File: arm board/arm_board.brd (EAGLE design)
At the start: 76.2 x 159.1 mm, 119 parts, among them J1 APPPP45_PCB_HORIZ_RIGHT, J10 SL02, J11 SL02, J12 SL02, J17 APPPP45_PCB_HORIZ_RIGHT, J18 APPPP45_PCB_HORIZ_RIGHT, J19 ENCODER, J2 APPPP45_PCB_HORIZ_RIGHT, J20 ENCODER, J21 ENCODER, J22 ENCODER, J24 ENCODER, J3 APPPP45_PCB_HORIZ_RIGHT, J5 SERVOMOLEX_SL_VERT_TH, J6 SL02, J7 SL02, J8 SL02, J9 SL02, Q1 Q_IRF7437SMD, U1 TIVA-1294

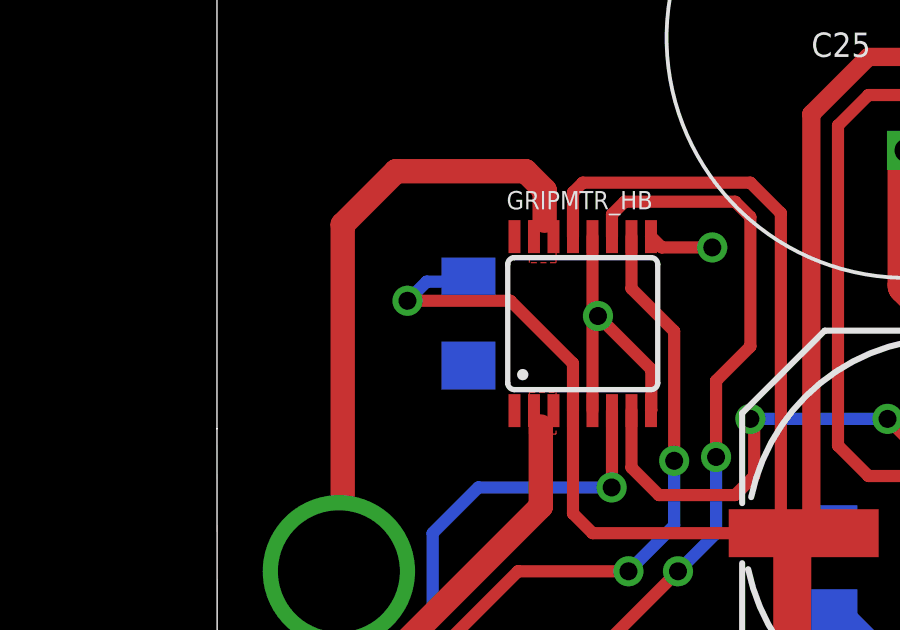
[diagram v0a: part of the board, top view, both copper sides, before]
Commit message: Routed GripHBridge COM pins to ground
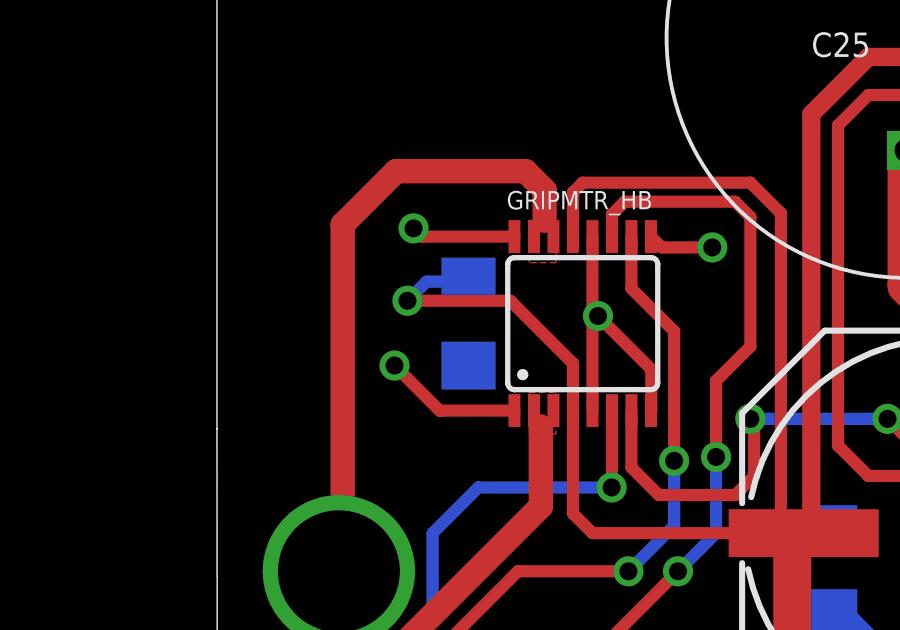
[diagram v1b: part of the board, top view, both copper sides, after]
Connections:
- net GND: now also GRIPMTR_HB.1, GRIPMTR_HB.16
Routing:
- net GND: track 169.0 -> 177.1 mm, vias 82 -> 84
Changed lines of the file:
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@@
 <wire x1="38.0748" y1="86.36" x2="37.4398" y2="86.995" width="0.8128" layer="1"/>
 <wire x1="37.4398" y1="86.995" x2="36.2458" y2="86.995" width="0.8128" layer="1"/>
+<contactref element="GRIPMTR_HB" pad="1"/>
+<contactref element="GRIPMTR_HB" pad="16"/>
+<wire x1="9.7138" y1="136.165" x2="7.218" y2="136.165" width="0.4064" layer="1"/>
+<wire x1="7.218" y1="136.165" x2="5.715" y2="137.668" width="0.4064" layer="1"/>
+<via x="5.715" y="137.668" extent="1-16" drill="0.6" shape="square"/>
+<wire x1="9.7138" y1="141.965" x2="6.625" y2="141.965" width="0.4064" layer="1"/>
+<wire x1="6.625" y1="141.965" x2="6.35" y2="142.24" width="0.4064" layer="1"/>
+<via x="6.35" y="142.24" extent="1-16" drill="0.6" shape="square"/>
 </signal>
 <signal name="LOG_PWR_12V">

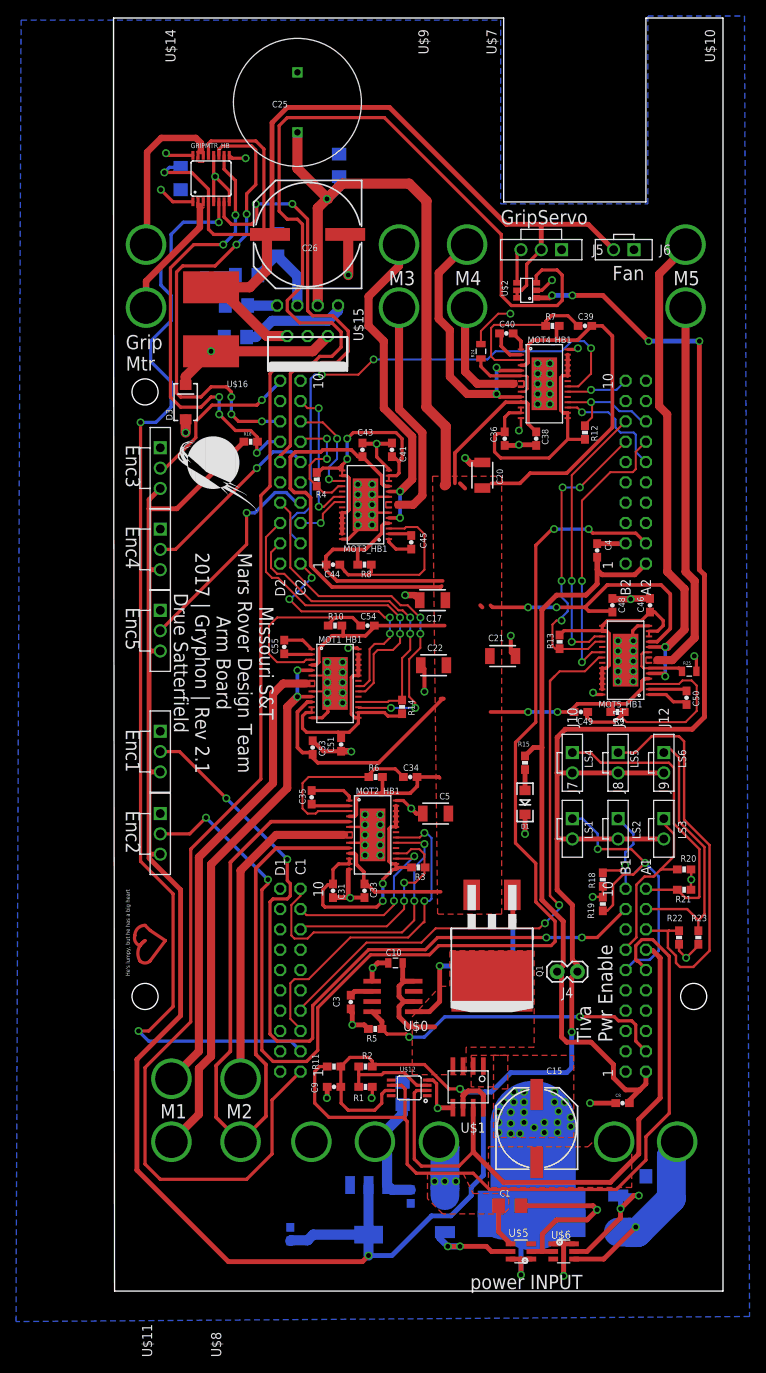
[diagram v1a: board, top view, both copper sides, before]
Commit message: Changed 8050 to 8010. 5V fan changed to 12V fan.
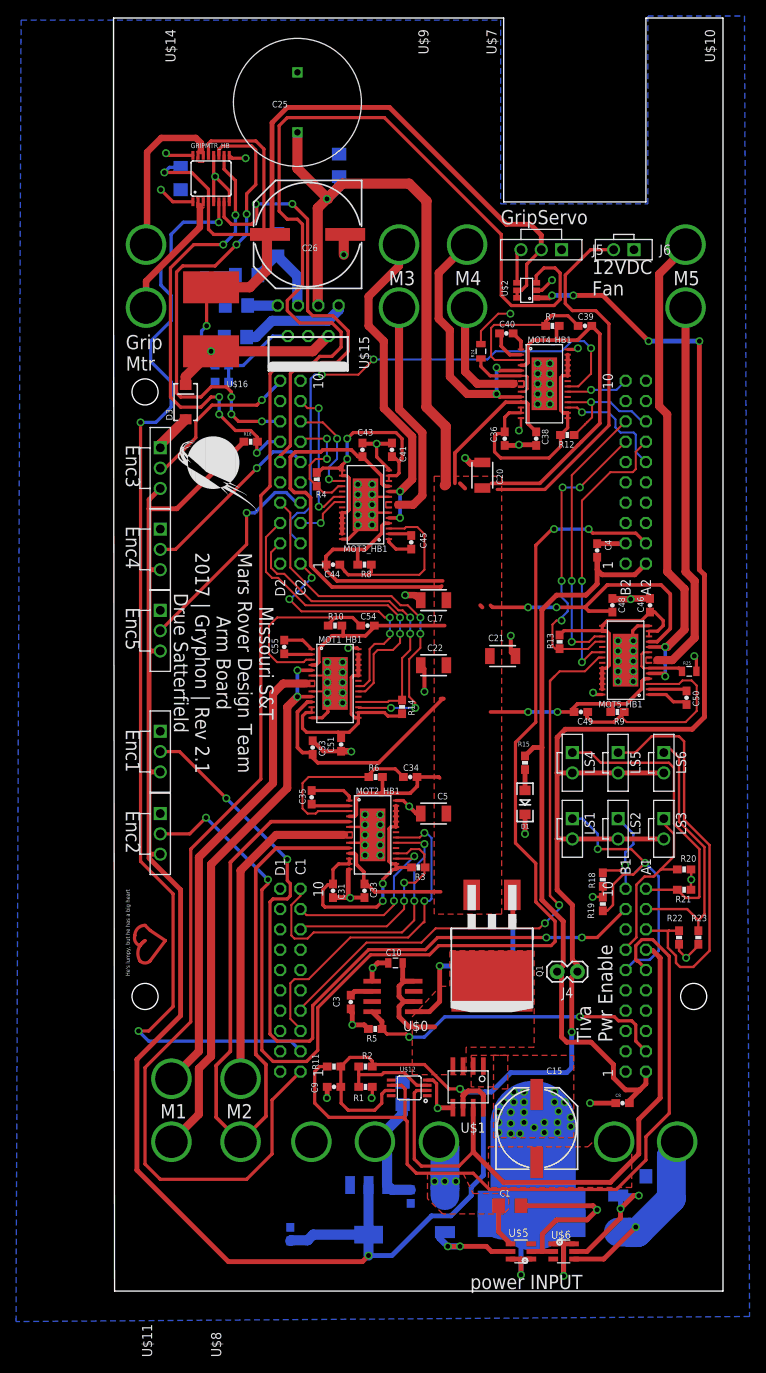
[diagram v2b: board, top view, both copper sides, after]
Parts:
- added R26: 12k, SparkFun-Passives:0603-RES
- added R27: 2k, SparkFun-Passives:0603-RES
- U$15: value SI-8050Y -> SI-8010Y; device opamps:TO-220-7 -> MRDT-ICs:TO-220-7
- moved R12 2.23 mm to (56.5, 107.0), turned to 180 degrees
- moved C5 0.25 mm to (39.8, 59.7)
- moved C17 0.13 mm to (39.8, 86.4)
- moved U$15 0.08 mm to (24.1, 119.4)
- renumbered J10 to LS4, J11 to LS5, J12 to LS6, J7 to LS1, J8 to LS2, J9 to LS3
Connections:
- removed net 5VMTR_PWR: C14.2, C26.+, GRIPMTR_HB.13, GRIPMTR_HB.4, J5.2, J6.2, U$15.6, U$16.P$2, U$2.5, U$2.6
- new net 7VMTR_PWR: C14.2, C26.+, GRIPMTR_HB.13, GRIPMTR_HB.4, J5.2, R26.1, U$16.P$2, U$2.5, U$2.6
- new net N$10: R26.2, R27.1, U$15.6
- net 12VMTR_PWR: now also J6.2
- net GND: now also R27.2
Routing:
- net 5VMTR_PWR: track 142.0 -> 0.00 mm, vias 1 -> 0
- net 7VMTR_PWR: track 0.00 -> 131.5 mm, vias 0 -> 2
- net 12VMTR_PWR: track 365.3 -> 409.5 mm
- net N$10: track 0.00 -> 11.0 mm
- net HB_3.3_OUTPUT6: track 33.2 -> 31.1 mm
- net MOT4_NFAULT: track 14.2 -> 15.9 mm
- net GND: track 177.1 -> 177.5 mm, vias 84 -> 83
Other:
- board text added: "12VDC Fan"
- board text removed: "Fan"
- board text removed: "LS1"
- board text removed: "LS2"
- board text removed: "LS3"
- board text removed: "LS4"
- board text removed: "LS5"
- board text removed: "LS6"

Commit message: Added new regulator for the servo
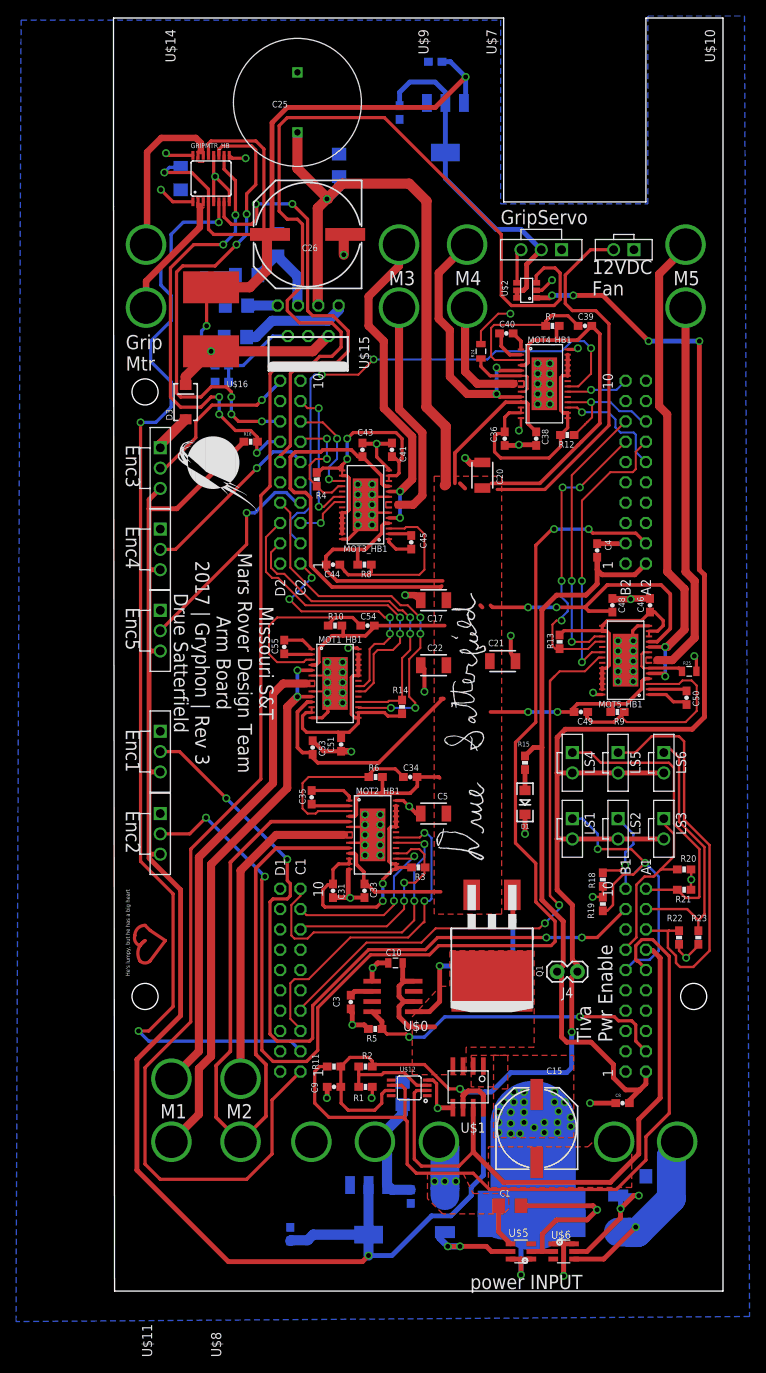
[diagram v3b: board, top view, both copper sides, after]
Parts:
- added C12: 1.0uF, SparkFun-Capacitors:0603-CAP
- added C13: 1uF, SparkFun-Capacitors:0603-CAP
- added U$17: SIG, drueLib:SIG
- added U$18: AZ1117EAZ1117EH-5.0, MRDT-ICs:SOT223
- moved C21 0.64 mm to (48.4, 78.7)
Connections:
- new net 5VSERVO_PWR: C13.1, J5.2, U$18.2, U$18.4, U$2.5, U$2.6
- net 7VMTR_PWR: now also C12.1, U$18.3; no longer J5.2, U$2.5, U$2.6
- net GND: now also C12.2, C13.2, U$18.1
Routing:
- net 5VSERVO_PWR: track 0.00 -> 42.7 mm
- net 7VMTR_PWR: track 131.5 -> 114.7 mm, vias 2 -> 3
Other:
- board text added: "Missouri S&T Mars Rover Design Team Arm Board 2017 | Gryphon | Rev 3 Drue Satterfield"
- board text removed: "Missouri S&T Mars Rover Design Team Arm Board 2017 | Gryphon | Rev 2.1 Drue Satterfield"

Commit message: Text editting
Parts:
- moved C30 0.64 mm to (15.2, 123.8)
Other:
- board text removed: "motor1"
- board text removed: "motor2"
- board text removed: "motor3"
- board text removed: "motor4"
- board text removed: "motor5"
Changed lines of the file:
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@@
 <wire x1="-0.2032" y1="159.131" x2="-0.2032" y2="135.56" width="0" layer="20"/>
 <wire x1="-0.2032" y1="135.56" x2="-0.0762" y2="0" width="0" layer="20"/>
-<text x="26.4668" y="3.556" size="1.778" layer="26" rot="MR0">Gnd</text>
-<text x="34.7218" y="3.556" size="1.778" layer="26" rot="MR0">logic</text>
-<text x="42.3418" y="3.556" size="1.778" layer="26" rot="MR0">act</text>
+<text x="21.209" y="16.0782" size="1.778" layer="25" rot="R90">Gnd</text>
+<text x="29.083" y="15.4432" size="1.778" layer="25" rot="R90">logic</text>
+<text x="36.957" y="16.2052" size="1.778" layer="25" rot="R90">act</text>
 <text x="13.5636" y="78.5114" size="1.778" layer="25" font="vector" rot="SR270" align="center">Missouri S&amp;T
 Mars Rover Design Team
@@
 Drue Satterfield</text>
 <text x="44.3738" y="0.254" size="1.778" layer="25" font="vector">power INPUT</text>
-<text x="73.4568" y="5.461" size="1.778" layer="26" rot="MR0">extra</text>
-<text x="64.5668" y="5.461" size="1.778" layer="26" rot="MR0">Gnd</text>
-<text x="7.7978" y="10.033" size="1.778" layer="26" rot="MR270">motor1</text>
-<text x="66.7258" y="139.319" size="1.778" layer="26" font="vector" rot="MR180">motor5</text>
-<text x="31.8008" y="136.779" size="1.778" layer="26" rot="MR180">motor3</text>
-<text x="16.6878" y="10.033" size="1.778" layer="26" rot="MR270">motor2</text>
-<text x="40.0558" y="136.779" size="1.778" layer="26" rot="MR180">motor4</text>
+<text x="74.549" y="15.4432" size="1.778" layer="25" rot="R90">extra</text>
+<text x="66.929" y="16.0782" size="1.778" layer="25" rot="R90">Gnd</text>
 <text x="1.3208" y="70.231" size="1.778" layer="25" rot="SR270">Enc1</text>
 <text x="1.3208" y="60.071" size="1.778" layer="25" rot="SR270">Enc2</text>
@@
 Mtr</text>
 <text x="48.1838" y="133.35" size="1.778" layer="25">GripServo</text>
-<text x="59.6138" y="124.46" size="1.778" layer="25" font="vector">12VDC
+<text x="60.2488" y="123.19" size="1.778" layer="25" font="vector">12VDC
 Fan</text>
 <text x="62.1538" y="31.115" size="1.778" layer="25" rot="R90">Tiva
@@
 <attribute name="COLOR1" value="" x="74.2188" y="-9.525" size="1.778" layer="27" rot="R90" display="off"/>
 </element>
-<element name="C11" library="SparkFun-Capacitors" package="1206" value="2.2uF" x="67.7418" y="14.351" rot="MR0">
+<element name="C11" library="SparkFun-Capacitors" package="1206" value="2.2uF" x="67.7418" y="14.351" smashed="yes" rot="MR0">
 <attribute name="PROD_ID" value="CAP-10009" x="67.7418" y="14.351" size="1.778" layer="28" rot="MR0" display="off"/>
+<attribute name="NAME" x="69.0118" y="15.494" size="0.8128" layer="26" rot="MR0"/>
+<attribute name="VALUE" x="69.1388" y="12.827" size="0.4064" layer="28" rot="MR0"/>
 </element>
 <element name="R3" library="SparkFun-Passives" package="0603-RES" value="10k" x="37.8968" y="52.959" smashed="yes" rot="R180">
@@
 <element name="D1" library="SparkFun-LED" package="LED-1206" value="Yellow" x="51.2318" y="61.087" smashed="yes" rot="R270">
 <attribute name="PROD_ID" value="DIO-09909" x="51.2318" y="61.087" size="1.778" layer="27" rot="R270" display="off"/>
-<attribute name="NAME" x="50.7238" y="57.785" size="0.6096" layer="25" font="vector"/>
+<attribute name="NAME" x="50.7238" y="57.785" size="0.8128" layer="25" font="vector"/>
 <attribute name="VALUE" x="49.4538" y="62.103" size="0.4064" layer="27" rot="R270"/>
 </element>
 <element name="R15" library="SparkFun-Resistors" package="0603-RES@1" value="330" x="51.2318" y="66.04" smashed="yes" rot="R270">
 <attribute name="PROD_ID" value="RES-10646" x="51.2318" y="66.04" size="1.778" layer="27" rot="R270" display="off"/>
-<attribute name="NAME" x="50.3428" y="68.072" size="0.6096" layer="25" font="vector"/>
+<attribute name="NAME" x="50.3428" y="68.072" size="0.8128" layer="25" font="vector"/>
 <attribute name="VALUE" x="50.0888" y="67.056" size="0.4064" layer="27" font="vector" rot="R270"/>
 </element>
@@
 <attribute name="VALUE" x="53.975" y="36.7538" size="1.27" layer="27"/>
 </element>
-<element name="C8" library="SparkFun-Capacitors" package="0603-CAP" value="0.01uF" x="63.4238" y="23.495">
+<element name="C8" library="SparkFun-Capacitors" package="0603-CAP" value="0.01uF" x="63.4238" y="23.495" smashed="yes">
 <attribute name="PROD_ID" value="CAP-08604" x="63.4238" y="23.495" size="0.4064" layer="27" display="off"/>
+<attribute name="NAME" x="62.5348" y="24.257" size="0.8128" layer="25" font="vector"/>
+<attribute name="VALUE" x="62.4078" y="22.352" size="0.4064" layer="27" font="vector"/>
 </element>
 <element name="C25" library="MRDT-2014-All" package="C_16MM" value="2200uF" x="22.7838" y="148.59" smashed="yes" rot="R180">
@@
 <attribute name="VALUE" x="21.7678" y="132.207" size="0.4064" layer="28" rot="MR270"/>
 </element>
-<element name="C30" library="MRDT-EAGLE-Training" package="1206" value="4.7uF" x="15.1638" y="123.19" smashed="yes" rot="MR180">
-<attribute name="PROD_ID" value="CAP-09822" x="-8.9662" y="145.415" size="1.778" layer="28" rot="MR180" display="off"/>
-<attribute name="NAME" x="11.8618" y="121.92" size="0.8128" layer="26" font="vector" rot="MR90"/>
-<attribute name="VALUE" x="13.7668" y="124.714" size="0.4064" layer="28" rot="MR180"/>
+<element name="C30" library="MRDT-EAGLE-Training" package="1206" value="4.7uF" x="15.1638" y="123.825" smashed="yes" rot="MR180">
+<attribute name="PROD_ID" value="CAP-09822" x="-8.9662" y="146.05" size="1.778" layer="28" rot="MR180" display="off"/>
+<attribute name="NAME" x="11.8618" y="122.555" size="0.8128" layer="26" font="vector" rot="MR90"/>
+<attribute name="VALUE" x="13.7668" y="125.349" size="0.4064" layer="28" rot="MR180"/>
 </element>
 <element name="C32" library="MRDT-EAGLE-Training" package="1206" value="4.7uF" x="27.9908" y="140.716" smashed="yes" rot="MR270">
@@
 </element>
 <element name="U$14" library="mine" package="APP45_HORIZ_CONFIG" value="APP45_HORIZ" x="-0.0762" y="159.004" rot="R270"/>
-<element name="R16" library="SparkFun-Passives" package="0603-RES" value="10k" x="16.9418" y="106.172"/>
+<element name="R16" library="SparkFun-Passives" package="0603-RES" value="10k" x="16.9418" y="106.172" smashed="yes">
+<attribute name="NAME" x="16.0528" y="106.934" size="0.8128" layer="25" font="vector"/>
+<attribute name="VALUE" x="15.9258" y="105.029" size="0.4064" layer="27" font="vector"/>
+</element>
 <element name="J5" library="MRDT-Connectors" package="MOLEX-70543-0002" value="SERVOMOLEX_SL_VERT_TH" x="53.2638" y="130.175" smashed="yes"/>
 <element name="J6" library="MRDT-Connectors" package="MOLEX-70543-0001" value="SL02" x="63.5762" y="130.175" smashed="yes"/>
@@
 <wire x1="12.485" y1="115.697" x2="12.065" y2="115.57" width="0.4064" layer="16"/>
 <wire x1="12.065" y1="115.57" x2="10.795" y2="116.84" width="0.4064" layer="16"/>
-<wire x1="10.795" y1="116.84" x2="10.795" y2="120.015" width="0.4064" layer="16"/>
-<wire x1="10.795" y1="120.015" x2="11.43" y2="120.65" width="0.4064" layer="16"/>
-<via x="11.43" y="120.65" extent="1-16" drill="0.6"/>
-<wire x1="11.43" y1="120.65" x2="11.43" y2="124.9162" width="0.4064" layer="1"/>
+<wire x1="10.795" y1="116.84" x2="10.795" y2="121.285" width="0.4064" layer="16"/>
+<via x="11.43" y="121.92" extent="1-16" drill="0.6"/>
+<wire x1="11.43" y1="121.92" x2="11.43" y2="124.9162" width="0.4064" layer="1"/>
 <wire x1="11.43" y1="124.9162" x2="11.9888" y2="125.475" width="0.4064" layer="1"/>
 <contactref element="U$18" pad="3"/>
@@
 <wire x1="40.855" y1="153.67" x2="41.91" y2="153.67" width="0.6096" layer="16"/>
 <wire x1="41.91" y1="153.67" x2="43.815" y2="151.765" width="0.6096" layer="16"/>
+<wire x1="10.795" y1="121.285" x2="11.43" y2="121.92" width="0.4064" layer="16"/>
 </signal>
 <signal name="N$9">
 <contactref element="C30" pad="2"/>
 <contactref element="U$15" pad="7"/>
-<wire x1="16.5638" y1="123.19" x2="20.32" y2="123.19" width="1.27" layer="16"/>
+<wire x1="20.32" y1="123.19" x2="17.1988" y2="123.19" width="1.27" layer="16"/>
+<wire x1="17.1988" y1="123.19" x2="16.5638" y2="123.825" width="1.27" layer="16"/>
 </signal>
 <signal name="N$13">
